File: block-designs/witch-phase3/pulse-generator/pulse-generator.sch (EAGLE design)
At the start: 91 parts, among them IC1 74LVC1G17DBV, IC10 74LVC1G08DBV, IC11 74LVC1G08DBV, IC12 741G175, IC13 741G175, IC14 741G175, IC15 741G175, IC16 741G175, IC17 74LVC1G04DBV, IC18 74LVC1G04DBV, IC19 74LVC1G08DBV, IC2 74LVC1G17DBV, IC20 74LVC1G04DBV, IC21 74LVC1G08DBV, IC22 741G175, IC23 74LVC1G08DBV, IC3 74LVC1G17DBV, IC4 NE555D, IC5 741G175, IC6 74LVC1G04DBV, IC7 74LVC1G04DBV, IC8 741G175, IC9 741G175, J1 POWER_JACKPTH, Q1 MMBT2222A, Q2 MMBT2222A, Q3 MMBT2222A, Q4 MMBT2222A, Q5 MMBT2222A, Q6 MMBT2907ALT1SMD

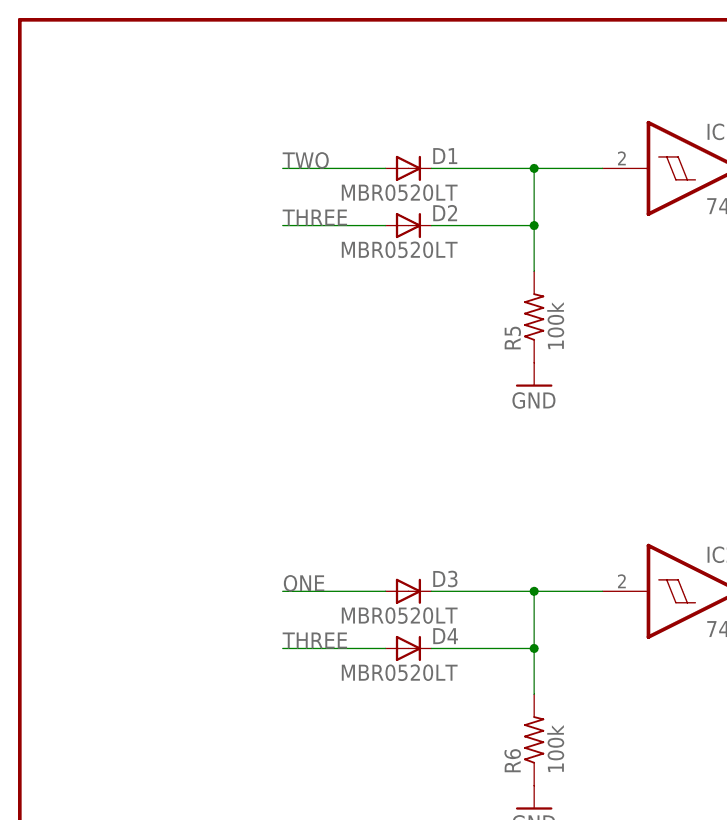
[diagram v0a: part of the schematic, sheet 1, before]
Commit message: update schematic and layout for off-by-one error on add/comp clr singals
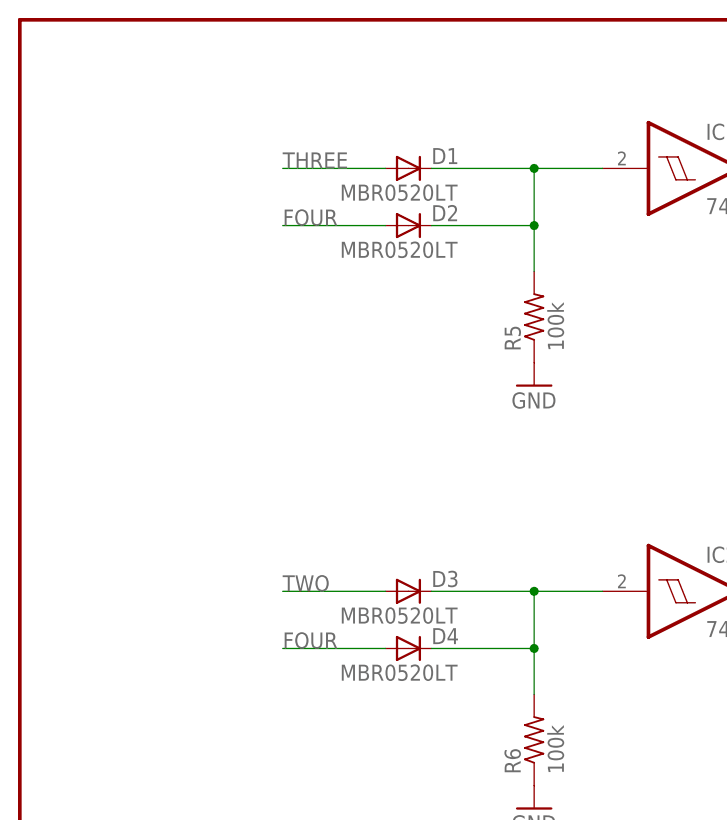
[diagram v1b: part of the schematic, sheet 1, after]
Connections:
- net FOUR: now also D2.A, D4.A
- net ONE: no longer D3.A
- net THREE: now also D1.A; no longer D2.A, D4.A
- net TWO: now also D3.A; no longer D1.A
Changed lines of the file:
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@@
 <net name="ONE" class="0">
-<segment>
-<pinref part="D3" gate="G$1" pin="A"/>
-<wire x1="40.64" y1="203.2" x2="29.21" y2="203.2" width="0.1524" layer="91"/>
-<label x="29.21" y="203.2" size="1.778" layer="95"/>
-</segment>
 <segment>
 <pinref part="JP5" gate="A" pin="3"/>
@@
 <net name="TWO" class="0">
 <segment>
-<pinref part="D1" gate="G$1" pin="A"/>
-<wire x1="40.64" y1="250.19" x2="29.21" y2="250.19" width="0.1524" layer="91"/>
-<label x="29.21" y="250.19" size="1.778" layer="95"/>
-</segment>
-<segment>
 <pinref part="JP5" gate="A" pin="4"/>
 <wire x1="381" y1="120.65" x2="342.9" y2="120.65" width="0.1524" layer="91"/>
 <label x="342.9" y="120.65" size="1.778" layer="95"/>
+</segment>
+<segment>
+<pinref part="D3" gate="G$1" pin="A"/>
+<wire x1="40.64" y1="203.2" x2="29.21" y2="203.2" width="0.1524" layer="91"/>
+<label x="29.21" y="203.2" size="1.778" layer="95"/>
 </segment>
 </net>
@@
 <net name="THREE" class="0">
 <segment>
-<pinref part="D4" gate="G$1" pin="A"/>
-<wire x1="40.64" y1="196.85" x2="29.21" y2="196.85" width="0.1524" layer="91"/>
-<label x="29.21" y="196.85" size="1.778" layer="95"/>
-</segment>
-<segment>
-<pinref part="D2" gate="G$1" pin="A"/>
-<wire x1="40.64" y1="243.84" x2="29.21" y2="243.84" width="0.1524" layer="91"/>
-<label x="29.21" y="243.84" size="1.778" layer="95"/>
-</segment>
-<segment>
 <pinref part="JP5" gate="A" pin="5"/>
 <wire x1="381" y1="123.19" x2="344.17" y2="123.19" width="0.1524" layer="91"/>
 <wire x1="342.9" y1="123.19" x2="344.17" y2="123.19" width="0.1524" layer="91"/>
 <label x="342.9" y="123.19" size="1.778" layer="95"/>
+</segment>
+<segment>
+<pinref part="D1" gate="G$1" pin="A"/>
+<wire x1="40.64" y1="250.19" x2="29.21" y2="250.19" width="0.1524" layer="91"/>
+<label x="29.21" y="250.19" size="1.778" layer="95"/>
 </segment>
 </net>
@@
 <label x="342.9" y="125.73" size="1.778" layer="95"/>
 </segment>
+<segment>
+<pinref part="D2" gate="G$1" pin="A"/>
+<wire x1="40.64" y1="243.84" x2="29.21" y2="243.84" width="0.1524" layer="91"/>
+<label x="29.21" y="243.84" size="1.778" layer="95"/>
+</segment>
+<segment>
+<pinref part="D4" gate="G$1" pin="A"/>
+<wire x1="40.64" y1="196.85" x2="29.21" y2="196.85" width="0.1524" layer="91"/>
+<label x="29.21" y="196.85" size="1.778" layer="95"/>
+</segment>
 </net>

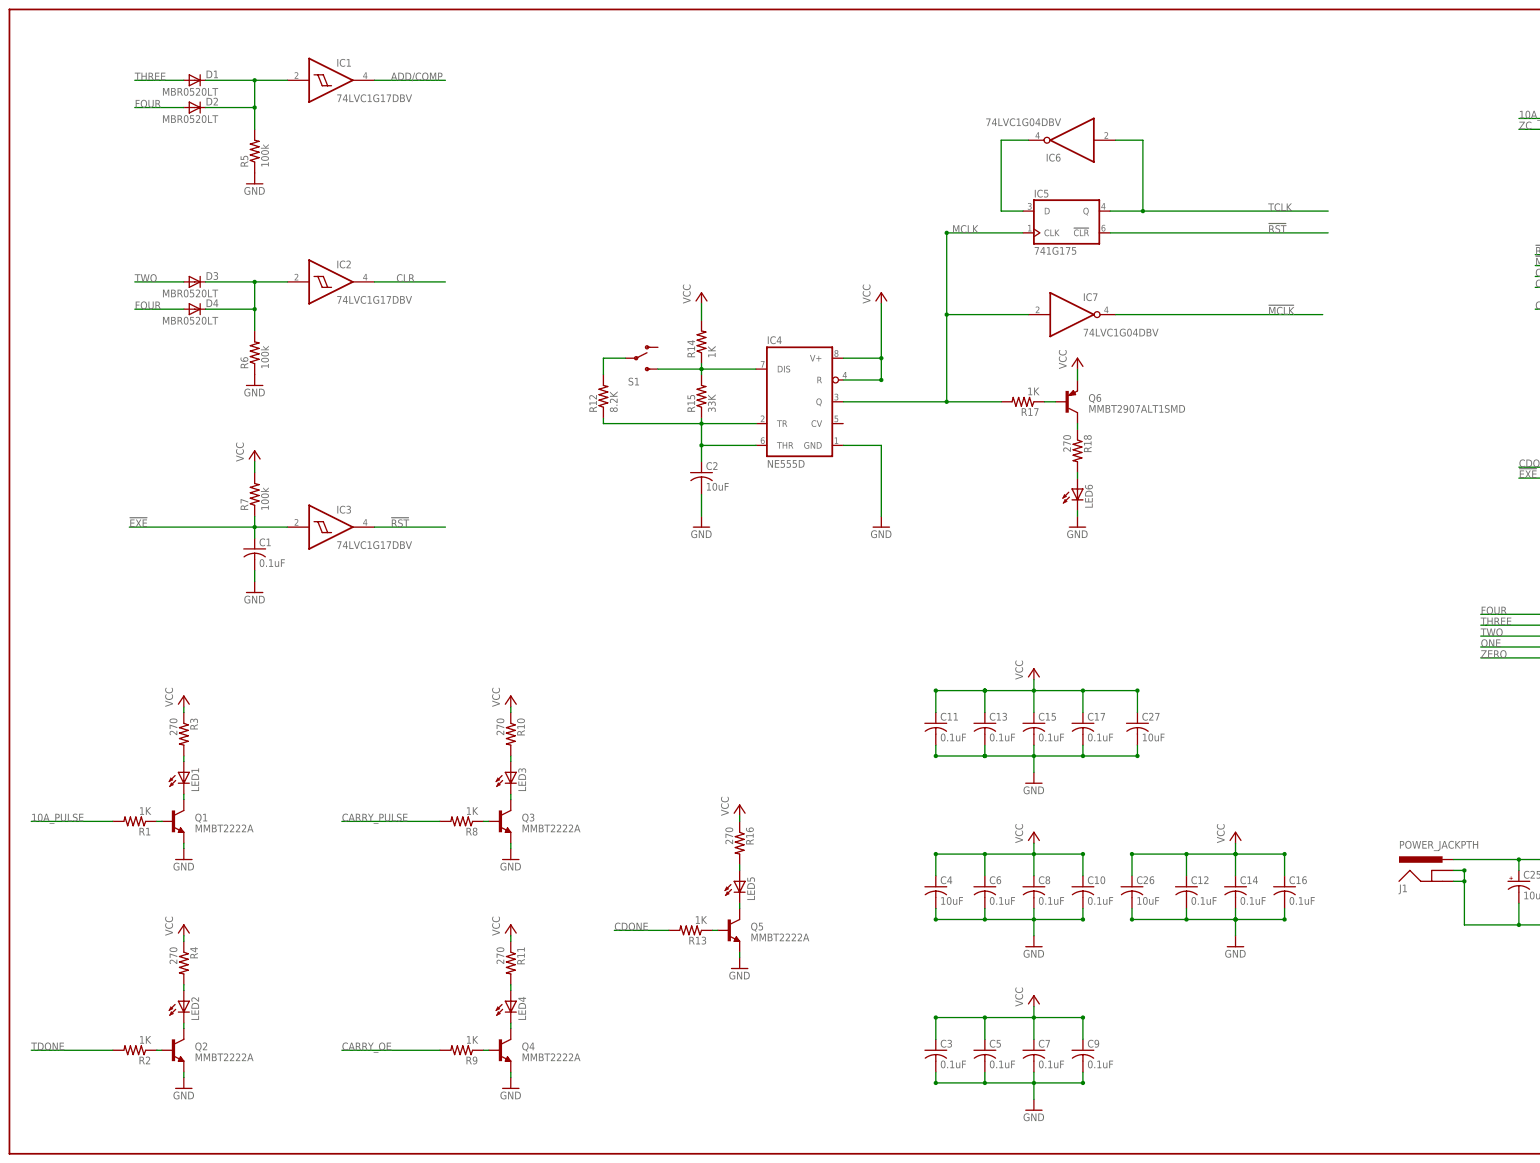
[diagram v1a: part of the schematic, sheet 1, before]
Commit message: add function select LEDs
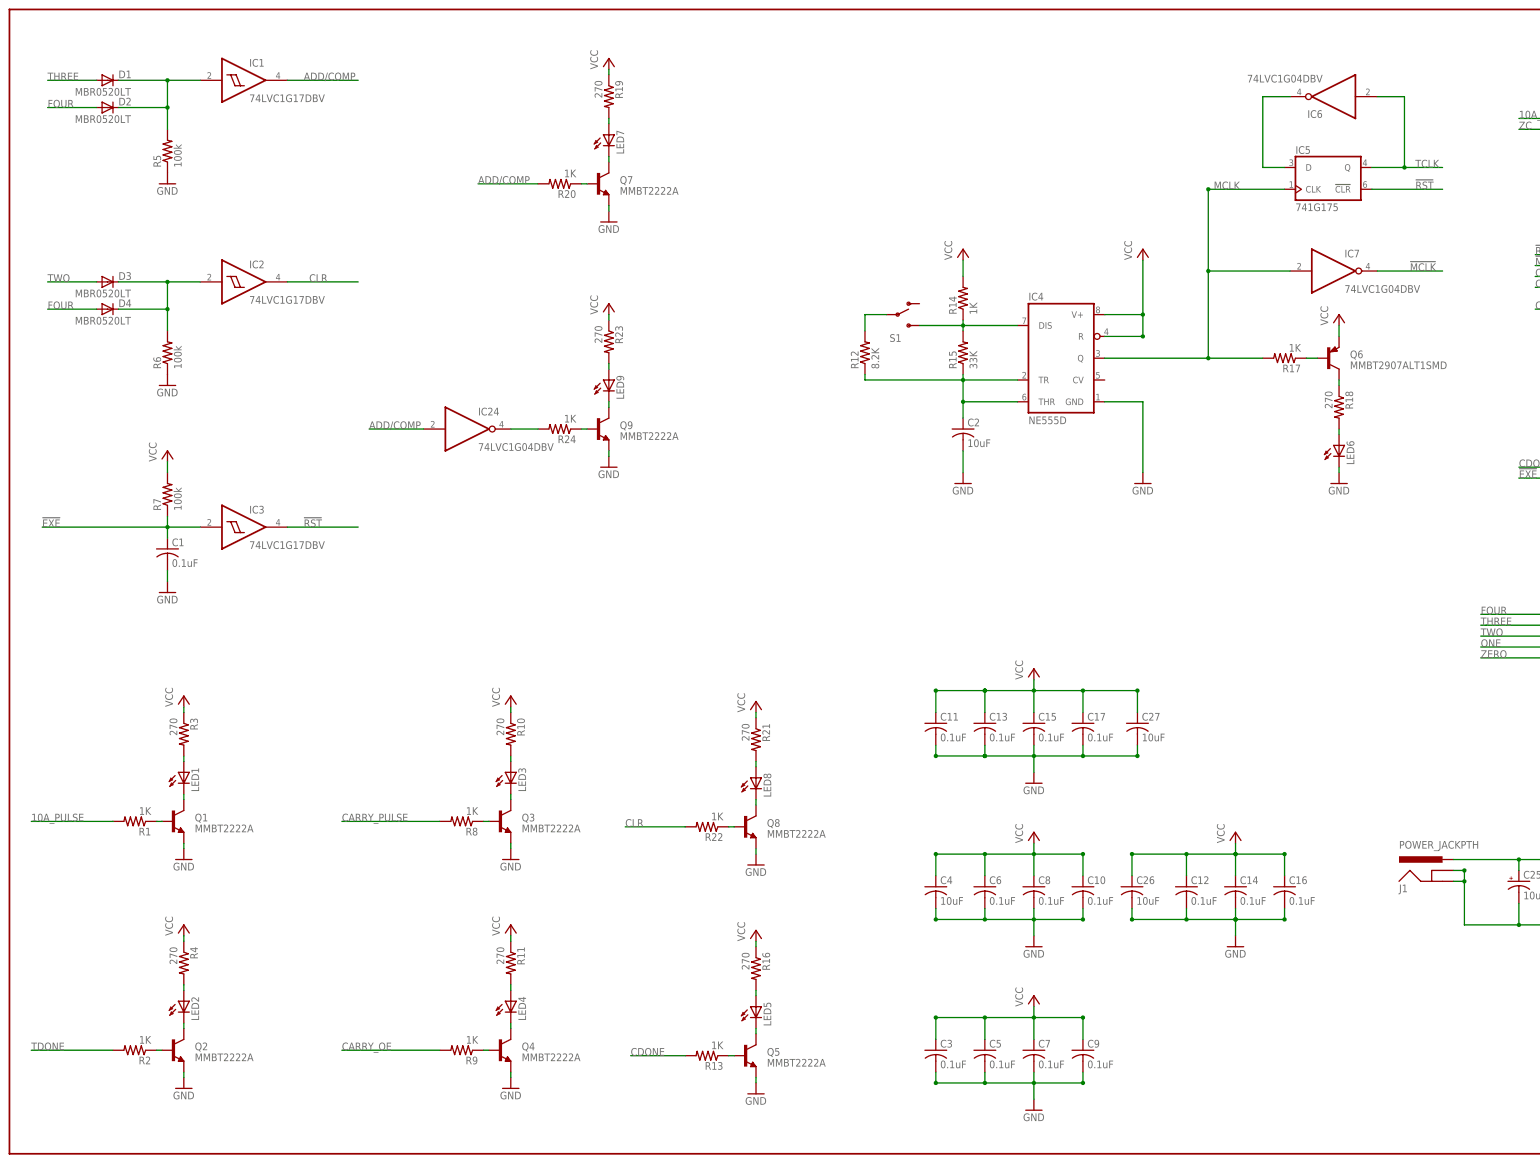
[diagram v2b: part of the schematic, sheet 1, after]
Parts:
- added IC24: 74LVC1G04DBV, 74xx-little-us:74LVC1G04DBV
- added LED7, LED8, LED9: (no value), led:LEDCHIP-LED0805
- added Q7, Q8, Q9: MMBT2222A, SparkFun-DiscreteSemi:TRANSISTOR_NPNMMBT2222A
- added R19, R21, R23: 270, resistor:R-US_R0805
- added R20, R22, R24: 1K, resistor:R-US_R0805
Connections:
- new net N$12: LED7.C, Q7.C
- new net N$14: Q7.B, R20.1
- new net N$20: LED7.A, R19.2
- new net N$21: LED8.C, Q8.C
- new net N$22: Q8.B, R22.1
- new net N$27: LED8.A, R21.2
- new net N$29: LED9.C, Q9.C
- new net N$30: Q9.B, R24.1
- new net N$40: LED9.A, R23.2
- new net N$41: IC24A.O, R24.2
- net ADD/COMP: now also IC24A.I, R20.2
- net CLR: now also R22.2
- net GND: now also Q7.E, Q8.E, Q9.E
- net VCC: now also R19.1, R21.1, R23.1
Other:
- moved on the sheet: C1, C2, D1, D2, D3, D4, IC1, IC2, IC3, IC4, IC5, IC6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

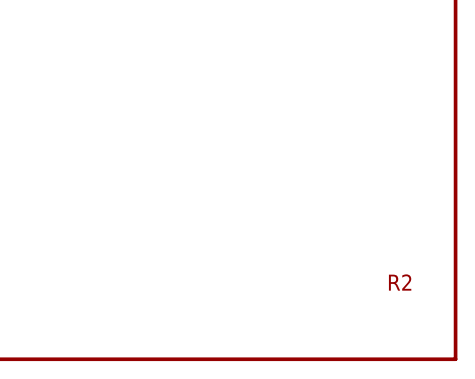
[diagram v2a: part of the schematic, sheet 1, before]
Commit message: add LEDs for functions and tweak layout
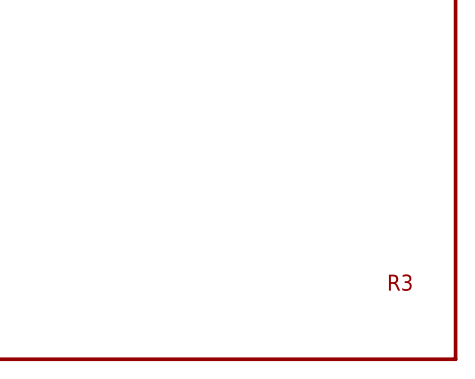
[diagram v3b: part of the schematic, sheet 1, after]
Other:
- note added: "R3"
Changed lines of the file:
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@@
 <sheet>
 <plain>
-<text x="393.7" y="7.62" size="1.778" layer="94">R2</text>
+<text x="393.7" y="7.62" size="1.778" layer="94">R3</text>
 </plain>
 <instances>
